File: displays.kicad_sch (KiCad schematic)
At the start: 34 parts, among them J10 LEDX, J11 LEDY, J7 TO-LCD, J9 PMOD, Q1 2N7002K, Q2 2N7002K, Q3 2N7002K, Q4 2N7002K, Q5 2N7002K, Q6 2N7002K, Q7 2N7002K, U11 74HC595D, U12 LTC-3743KD, U8 MAX7221xNG

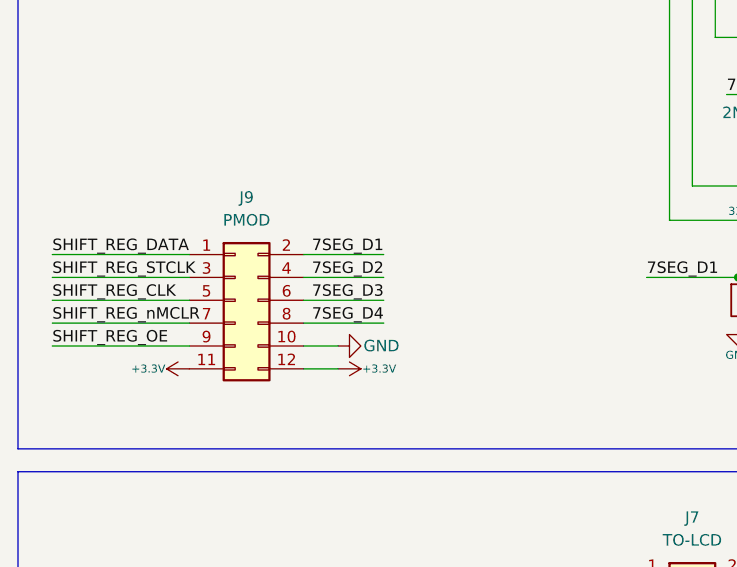
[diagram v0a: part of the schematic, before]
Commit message: Update the footprints
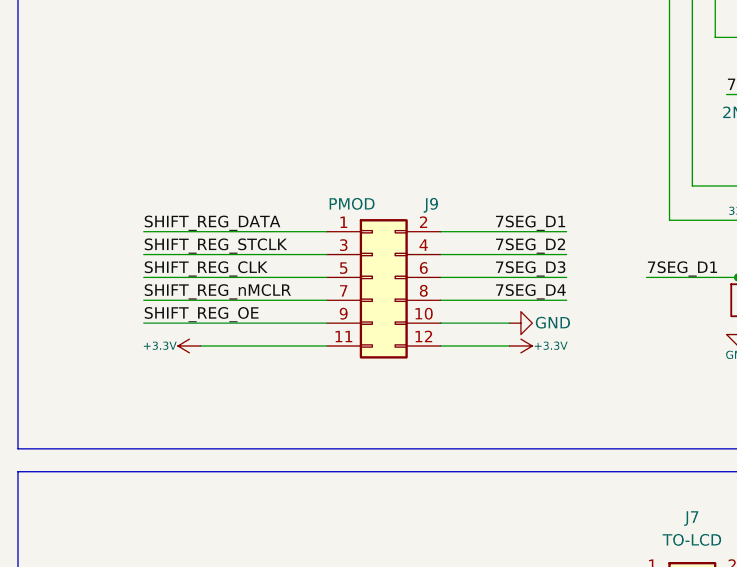
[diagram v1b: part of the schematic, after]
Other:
- moved on the sheet: J9
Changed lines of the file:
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@@
 	(wire
 		(pts
+			(xy 60.96 111.76) (xy 68.58 111.76)
+		)
+		(stroke
+			(width 0)
+			(type default)
+		)
+	)
+	(wire
+		(pts
 			(xy 74.93 44.45) (xy 93.98 44.45)
 		)
@@
 	(wire
 		(pts
-			(xy 54.61 106.68) (xy 45.72 106.68)
+			(xy 34.29 114.3) (xy 48.26 114.3)
 		)
 		(stroke
@@
 	(wire
 		(pts
-			(xy 17.78 106.68) (xy 33.02 106.68)
+			(xy 27.94 104.14) (xy 48.26 104.14)
 		)
 		(stroke
@@
 	(wire
 		(pts
-			(xy 54.61 109.22) (xy 45.72 109.22)
-		)
-		(stroke
-			(width 0)
-			(type default)
-		)
-	)
-	(wire
-		(pts
 			(xy 44.45 50.8) (xy 44.45 41.91)
 		)
@@
 	(wire
 		(pts
-			(xy 45.72 116.84) (xy 49.53 116.84)
-		)
-		(stroke
-			(width 0)
-			(type default)
-		)
-	)
-	(wire
-		(pts
 			(xy 93.98 106.68) (xy 95.25 106.68)
 		)
@@
 	(wire
 		(pts
-			(xy 17.78 109.22) (xy 33.02 109.22)
+			(xy 27.94 106.68) (xy 48.26 106.68)
 		)
 		(stroke
@@
 	(wire
 		(pts
-			(xy 54.61 104.14) (xy 45.72 104.14)
+			(xy 26.67 49.53) (xy 46.99 49.53)
 		)
 		(stroke
@@
 	(wire
 		(pts
-			(xy 26.67 49.53) (xy 46.99 49.53)
+			(xy 74.93 142.24) (xy 82.55 142.24)
 		)
 		(stroke
@@
 	(wire
 		(pts
-			(xy 74.93 142.24) (xy 82.55 142.24)
+			(xy 54.61 36.83) (xy 53.34 36.83)
 		)
 		(stroke
@@
 	(wire
 		(pts
-			(xy 54.61 36.83) (xy 53.34 36.83)
+			(xy 207.01 50.8) (xy 214.63 50.8)
 		)
 		(stroke
@@
 	(wire
 		(pts
-			(xy 207.01 50.8) (xy 214.63 50.8)
+			(xy 77.47 147.32) (xy 82.55 147.32)
 		)
 		(stroke
@@
 	(wire
 		(pts
-			(xy 77.47 147.32) (xy 82.55 147.32)
+			(xy 60.96 101.6) (xy 74.93 101.6)
 		)
 		(stroke
@@
 	(wire
 		(pts
-			(xy 45.72 114.3) (xy 49.53 114.3)
+			(xy 137.16 76.2) (xy 134.62 76.2)
 		)
 		(stroke
@@
 	(wire
 		(pts
-			(xy 137.16 76.2) (xy 134.62 76.2)
+			(xy 74.93 52.07) (xy 76.2 52.07)
 		)
 		(stroke
@@
 	(wire
 		(pts
-			(xy 74.93 52.07) (xy 76.2 52.07)
+			(xy 88.9 57.15) (xy 88.9 96.52)
 		)
 		(stroke
@@
 	(wire
 		(pts
-			(xy 88.9 57.15) (xy 88.9 96.52)
+			(xy 26.67 46.99) (xy 54.61 46.99)
 		)
 		(stroke
@@
 	(wire
 		(pts
-			(xy 26.67 46.99) (xy 54.61 46.99)
+			(xy 60.96 106.68) (xy 74.93 106.68)
 		)
 		(stroke
@@
 	(wire
 		(pts
-			(xy 17.78 114.3) (xy 33.02 114.3)
+			(xy 27.94 111.76) (xy 48.26 111.76)
 		)
 		(stroke
@@
 	(wire
 		(pts
-			(xy 46.99 49.53) (xy 54.61 49.53)
+			(xy 60.96 114.3) (xy 68.58 114.3)
 		)
 		(stroke
@@
 	(wire
 		(pts
-			(xy 46.99 33.02) (xy 50.8 33.02)
+			(xy 46.99 49.53) (xy 54.61 49.53)
 		)
 		(stroke
@@
 	(wire
 		(pts
-			(xy 54.61 111.76) (xy 45.72 111.76)
+			(xy 46.99 33.02) (xy 50.8 33.02)
 		)
 		(stroke
@@
 	(wire
 		(pts
+			(xy 60.96 109.22) (xy 74.93 109.22)
+		)
+		(stroke
+			(width 0)
+			(type default)
+		)
+	)
+	(wire
+		(pts
 			(xy 207.01 46.99) (xy 207.01 50.8)
 		)
@@
 	(wire
 		(pts
+			(xy 60.96 104.14) (xy 74.93 104.14)
+		)
+		(stroke
+			(width 0)
+			(type default)
+		)
+	)
+	(wire
+		(pts
 			(xy 120.65 82.55) (xy 129.54 82.55)
 		)
@@
 	(wire
 		(pts
-			(xy 17.78 111.76) (xy 33.02 111.76)
+			(xy 27.94 109.22) (xy 48.26 109.22)
 		)
 		(stroke
@@
 	(wire
 		(pts
-			(xy 17.78 104.14) (xy 33.02 104.14)
+			(xy 27.94 101.6) (xy 48.26 101.6)
 		)
 		(stroke
@@
 	)
 	(label "7SEG_D4"
-		(at 54.61 111.76 180)
+		(at 74.93 109.22 180)
 		(effects
 			(font
@@
 	)
 	(label "SHIFT_REG_STCLK"
-		(at 17.78 106.68 0)
+		(at 27.94 104.14 0)
 		(effects
 			(font
@@
 	)
 	(label "SHIFT_REG_CLK"
-		(at 17.78 109.22 0)
+		(at 27.94 106.68 0)
 		(effects
 			(font
@@
 	)
 	(label "SHIFT_REG_OE"
-		(at 17.78 114.3 0)
+		(at 27.94 111.76 0)
 		(effects
 			(font
@@
 	)
 	(label "7SEG_D1"
-		(at 54.61 104.14 180)
+		(at 74.93 101.6 180)
 		(effects
 			(font
@@
 	)
 	(label "7SEG_D2"
-		(at 54.61 106.68 180)
+		(at 74.93 104.14 180)
 		(effects
 			(font
@@
 	)
 	(label "7SEG_D3"
-		(at 54.61 109.22 180)
+		(at 74.93 106.68 180)
 		(effects
 			(font
@@
 	)
 	(label "SHIFT_REG_DATA"
-		(at 17.78 104.14 0)
+		(at 27.94 101.6 0)
 		(effects
 			(font
@@
 	)
 	(label "SHIFT_REG_nMCLR"
-		(at 17.78 111.76 0)
+		(at 27.94 109.22 0)
 		(effects
 			(font
@@
 	(symbol
 		(lib_id "power:GND")
-		(at 49.53 114.3 90)
+		(at 68.58 111.76 90)
 		(unit 1)
 		(exclude_from_sim no)
@@
 		(dnp no)
 		(property "Reference" "#PWR067"
-			(at 55.88 114.3 0)
+			(at 74.93 111.76 0)
 			(effects
 				(font
@@
 		)
 		(property "Value" "GND"
-			(at 54.356 114.3 90)
+			(at 73.406 111.76 90)
 			(effects
 				(font
@@
 		)
 		(property "Footprint" ""
-			(at 49.53 114.3 0)
+			(at 68.58 111.76 0)
 			(effects
 				(font
@@
 		)
 		(property "Datasheet" ""
-			(at 49.53 114.3 0)
+			(at 68.58 111.76 0)
 			(effects
 				(font
@@
 		)
 		(property "Description" "Power symbol creates a global label with name \"GND\" , ground"
-			(at 49.53 114.3 0)
+			(at 68.58 111.76 0)
 			(effects
 				(font
@@
 	(symbol
 		(lib_id "power:+3.3V")
-		(at 49.53 116.84 270)
+		(at 68.58 114.3 270)
 		(unit 1)
 		(exclude_from_sim no)
@@
 		(dnp no)
 		(property "Reference" "#PWR0156"
-			(at 45.72 116.84 0)
+			(at 64.77 114.3 0)
 			(effects
 				(font
@@
 		)
 		(property "Value" "+3.3V"
-			(at 54.102 116.84 90)
+			(at 73.152 114.3 90)
 			(effects
 				(font
@@
 		)
 		(property "Footprint" ""
-			(at 49.53 116.84 0)
+			(at 68.58 114.3 0)
 			(effects
 				(font
@@
 		)
 		(property "Datasheet" ""
-			(at 49.53 116.84 0)
+			(at 68.58 114.3 0)
 			(effects
 				(font
@@
 		)
 		(property "Description" "Power symbol creates a global label with name \"+3.3V\""
-			(at 49.53 116.84 0)
+			(at 68.58 114.3 0)
 			(effects
 				(font
@@
 	(symbol
 		(lib_id "Connector_Generic:Conn_02x06_Odd_Even")
-		(at 38.1 109.22 0)
+		(at 53.34 106.68 0)
 		(unit 1)
 		(exclude_from_sim no)
@@
 		(on_board yes)
 		(dnp no)
-		(fields_autoplaced yes)
 		(property "Reference" "J9"
-			(at 39.37 97.79 0)
+			(at 59.944 98.552 0)
 			(effects
 				(font
@@
 		)
 		(property "Value" "PMOD"
-			(at 39.37 100.33 0)
+			(at 51.054 98.552 0)
 			(effects
 				(font
@@
 		)
 		(property "Footprint" "Connector_PinSocket_2.54mm:PinSocket_2x06_P2.54mm_Vertical"
-			(at 38.1 109.22 0)
+			(at 53.34 106.68 0)
 			(effects
 				(font
@@
 		)
 		(property "Datasheet" "~"
-			(at 38.1 109.22 0)
+			(at 53.34 106.68 0)
 			(effects
 				(font
@@
 		)
 		(property "Description" "Generic connector, double row, 02x06, odd/even pin numbering scheme (row 1 odd numbers, row 2 even numbers), script generated (kicad-library-utils/schlib/autogen/connector/)"
-			(at 38.1 109.22 0)
+			(at 53.34 106.68 0)
 			(effects
 				(font
@@
 	(symbol
 		(lib_id "power:+3.3V")
-		(at 33.02 116.84 90)
+		(at 34.29 114.3 90)
 		(unit 1)
 		(exclude_from_sim no)
@@
 		(dnp no)
 		(property "Reference" "#PWR066"
-			(at 36.83 116.84 0)
+			(at 38.1 114.3 0)
 			(effects
 				(font
@@
 		)
 		(property "Value" "+3.3V"
-			(at 28.448 116.84 90)
+			(at 29.718 114.3 90)
 			(effects
 				(font
@@
 		)
 		(property "Footprint" ""
-			(at 33.02 116.84 0)
+			(at 34.29 114.3 0)
 			(effects
 				(font
@@
 		)
 		(property "Datasheet" ""
-			(at 33.02 116.84 0)
+			(at 34.29 114.3 0)
 			(effects
 				(font
@@
 		)
 		(property "Description" "Power symbol creates a global label with name \"+3.3V\""
-			(at 33.02 116.84 0)
+			(at 34.29 114.3 0)
 			(effects
 				(font

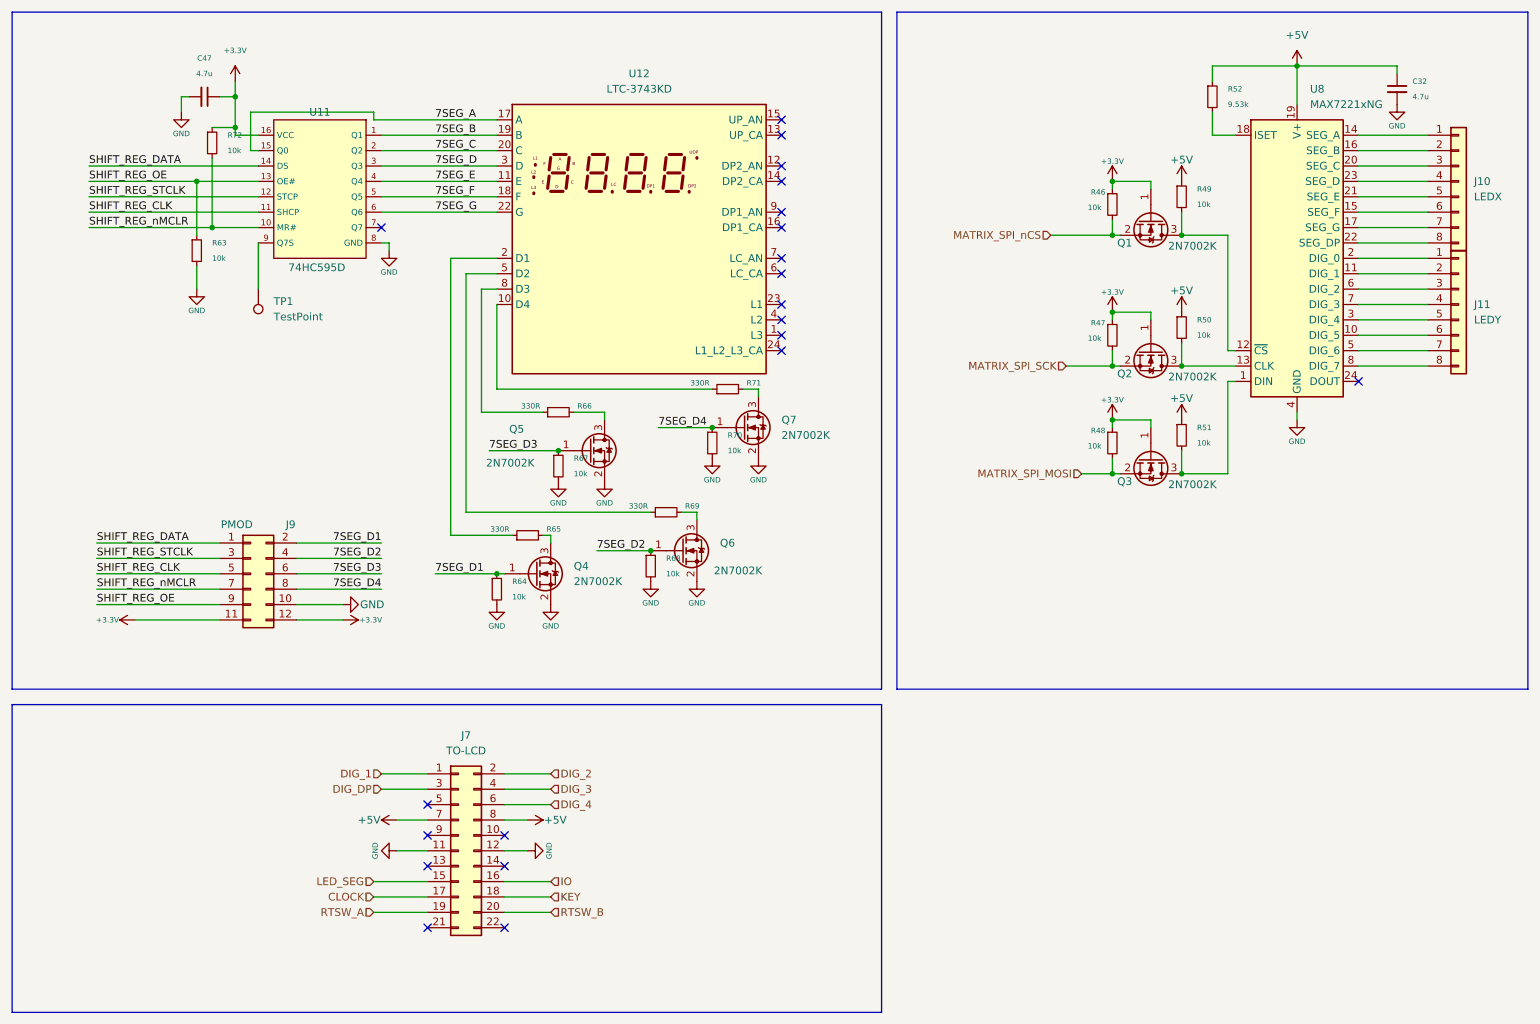
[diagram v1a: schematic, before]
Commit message: Update the BOM and the routing
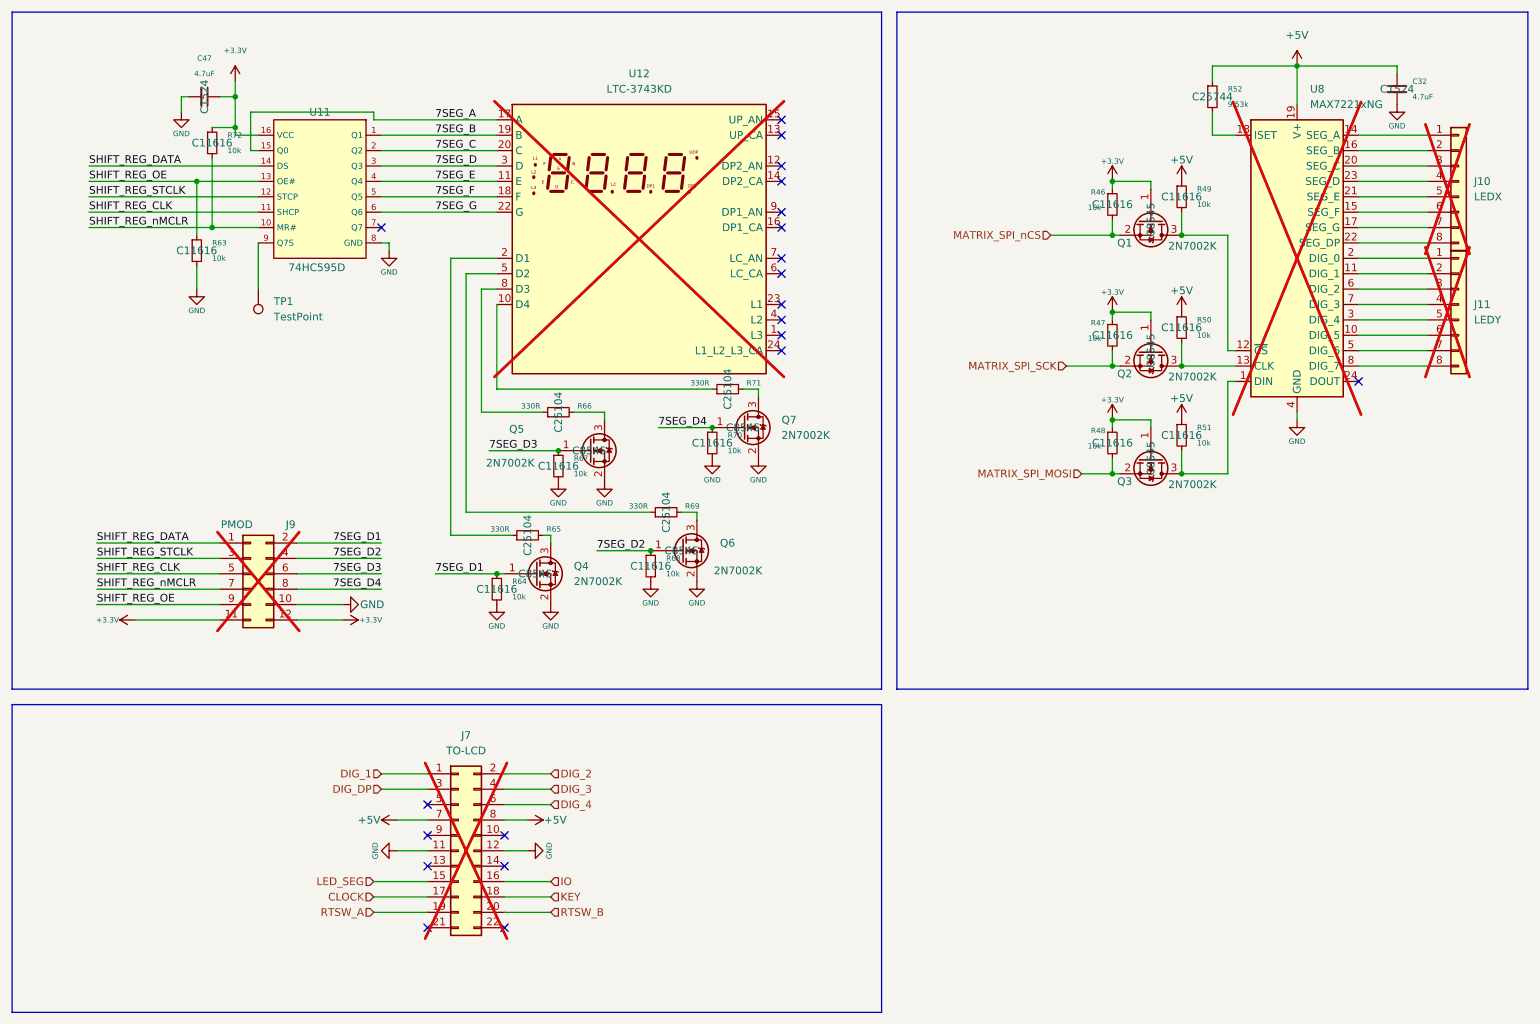
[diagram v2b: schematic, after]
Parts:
- C32, C47: value 4.7u -> 4.7uF; LCSC (none) -> C1524
- J10, J11, J7, J9, U12, U8: now not fitted; now left out of the parts list
- Q1, Q2, Q3, Q4, Q5, Q6, Q7: LCSC (none) -> C8545
- R46, R47, R48, R49, R50, R51, R63, R64, R67, R68, R70, R72: LCSC (none) -> C11616
- R52: LCSC (none) -> C25744
- R65, R66, R69, R71: LCSC (none) -> C25104
- U11: Attrition Qty 0 -> (none); Category Logic ICs,Registers -> (none); Class Basic Component -> (none); Function 串行至并行或串行 -> (none); Minimum Qty 1 -> (none); Number Of Bits Per Element 8 -> (none); Operating Temperature 40°C~+125°C -> (none); Output Type Tri-State -> (none); Part 74HC595D,118 -> (none); Price 0.133USD -> (none); Process SMT -> (none); Series 74HC -> (none); Stock 83301 -> (none); Supply Voltage 2V~6V -> (none)
